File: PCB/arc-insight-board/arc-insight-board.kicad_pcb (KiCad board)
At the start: 2 copper layers, 14.1 x 69.5 mm, 41 parts, among them J1 USB_C_Receptacle, J2 Conn_01x06, J3 Conn_01x05, J4 Conn_01x02, J5 Conn_01x02, J6 FPC_24PIN, J7 Conn_01x02, J8 U.FL, M1 Electret, U1 ESP32-S3, U2 MAX98357A, U3 MAX98357A, U4 TP4054, U5 Comparator, U6 ME6211C33M5, Y1 40MHz

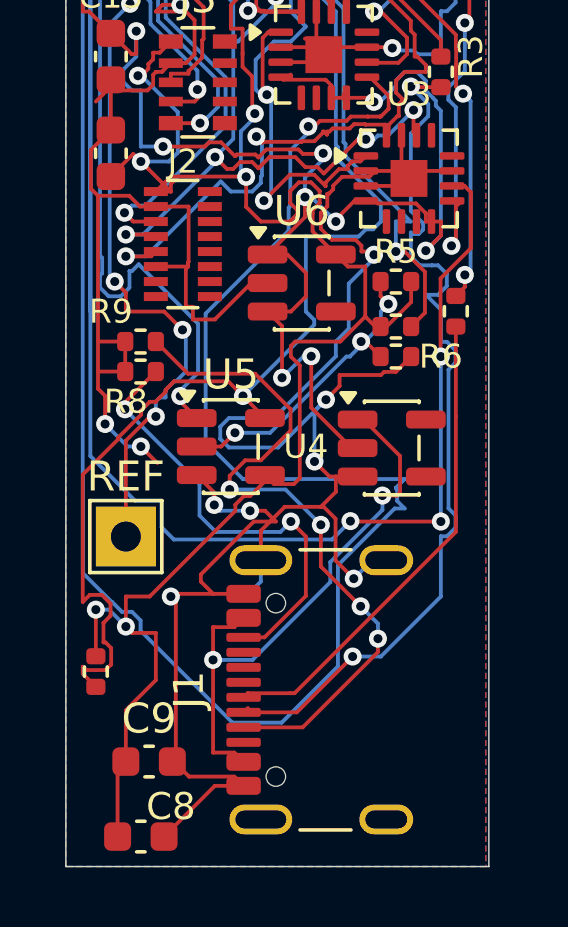
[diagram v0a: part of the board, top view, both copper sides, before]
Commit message: Fix J1 position, rotate U4/U6 to correct orientation
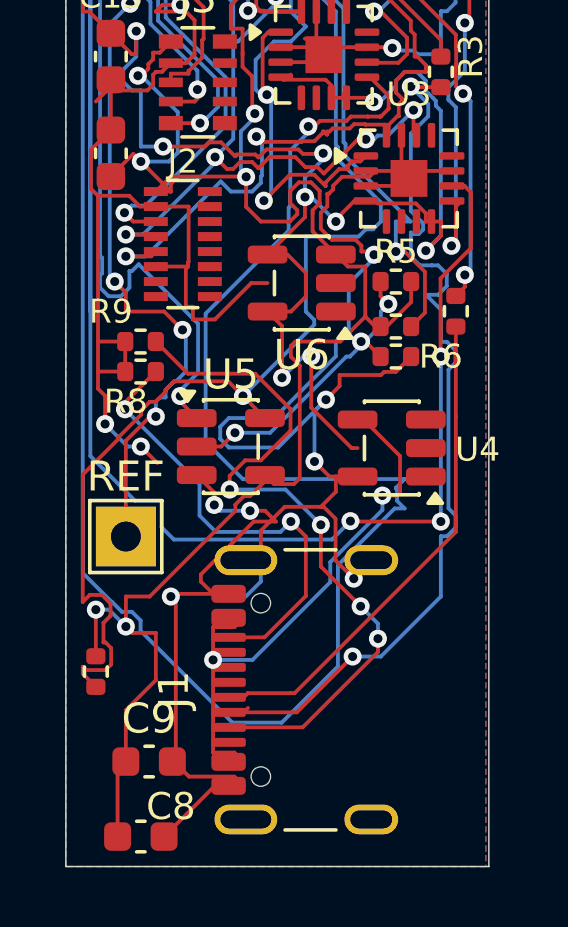
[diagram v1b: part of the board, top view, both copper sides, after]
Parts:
- moved J1 0.50 mm to (140.6, 136.6)
- turned U4 to 180 degrees
- turned U6 to 180 degrees
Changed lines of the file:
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@@
 	(footprint "Connector_USB:USB_C_Receptacle_GCT_USB4105-xx-A_16P_TopMnt_Horizontal"
 		(layer "F.Cu")
-		(at 141.105 136.61 90)
+		(at 140.605 136.61 90)
 		(descr "USB 2.0 Type C Receptacle, GCT, 16P, top mounted, horizontal, 5A: https://gct.co/files/drawings/usb4105.pdf")
 		(tags "USB C Type-C Receptacle SMD USB 2.0 16P 16C USB4105-15-A USB4105-15-A-060 USB4105-15-A-120 USB4105-GF-A USB4105-GF-A-060 USB4105-GF-A-120")
@@
 	(footprint "Package_TO_SOT_SMD:SOT-23-5"
 		(layer "F.Cu")
-		(at 142.3625 128.55)
+		(at 142.3625 128.55 180)
 		(descr "SOT, 5 Pin (JEDEC MO-178 Var AA https://www.jedec.org/document_search?search_api_views_fulltext=MO-178)")
 		(tags "SOT TO_SOT_SMD")
@@
 	(footprint "Package_TO_SOT_SMD:SOT-23-5"
 		(layer "F.Cu")
-		(at 139.3625 123.05)
+		(at 139.3625 123.05 180)
 		(descr "SOT, 5 Pin (JEDEC MO-178 Var AA https://www.jedec.org/document_search?search_api_views_fulltext=MO-178)")
 		(tags "SOT TO_SOT_SMD")

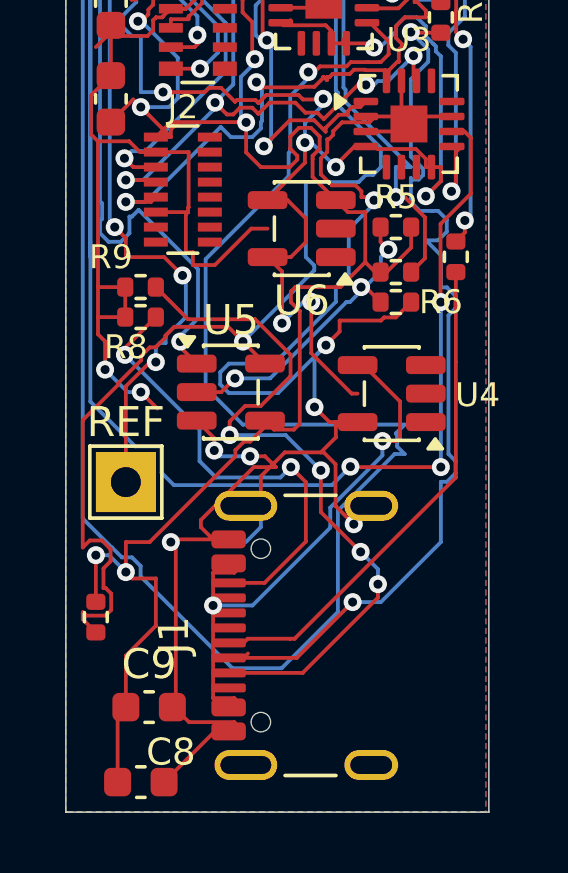
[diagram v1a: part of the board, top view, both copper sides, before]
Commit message: Adjust J1, U5, U6 rotations/position per request
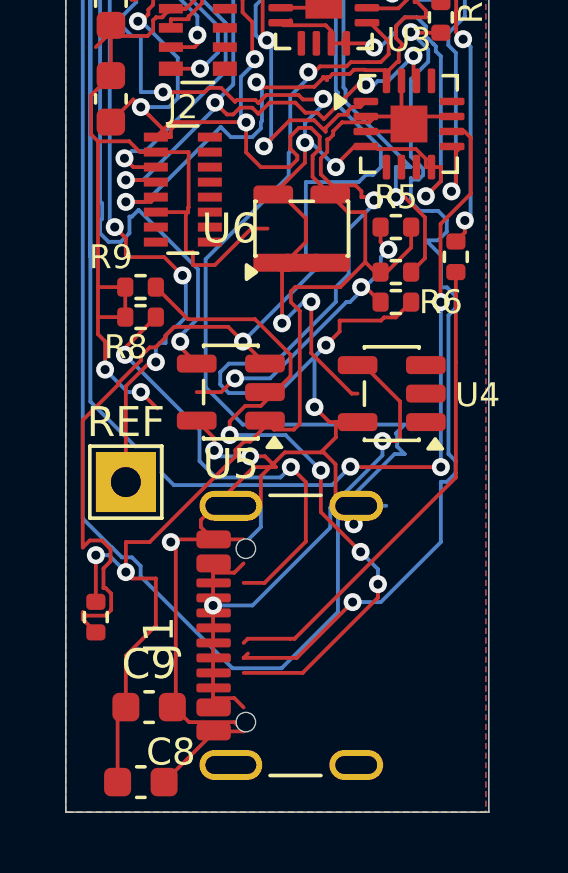
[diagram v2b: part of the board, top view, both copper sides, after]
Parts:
- moved J1 0.50 mm to (140.1, 136.6)
- turned U5 to 180 degrees
- turned U6 to 90 degrees
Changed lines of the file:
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@@
 	(footprint "Connector_USB:USB_C_Receptacle_GCT_USB4105-xx-A_16P_TopMnt_Horizontal"
 		(layer "F.Cu")
-		(at 140.605 136.61 90)
+		(at 140.105 136.61 90)
 		(descr "USB 2.0 Type C Receptacle, GCT, 16P, top mounted, horizontal, 5A: https://gct.co/files/drawings/usb4105.pdf")
 		(tags "USB C Type-C Receptacle SMD USB 2.0 16P 16C USB4105-15-A USB4105-15-A-060 USB4105-15-A-120 USB4105-GF-A USB4105-GF-A-060 USB4105-GF-A-120")
@@
 	(footprint "Package_TO_SOT_SMD:SOT-23-5"
 		(layer "F.Cu")
-		(at 139.3625 123.05 180)
+		(at 139.3625 123.05 90)
 		(descr "SOT, 5 Pin (JEDEC MO-178 Var AA https://www.jedec.org/document_search?search_api_views_fulltext=MO-178)")
 		(tags "SOT TO_SOT_SMD")
@@
 	(footprint "Package_TO_SOT_SMD:SOT-23-5"
 		(layer "F.Cu")
-		(at 137 128.5)
+		(at 137 128.5 180)
 		(descr "SOT, 5 Pin (JEDEC MO-178 Var AA https://www.jedec.org/document_search?search_api_views_fulltext=MO-178)")
 		(tags "SOT TO_SOT_SMD")

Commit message: Rotate U6 180 degrees
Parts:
- turned U6 to 270 degrees
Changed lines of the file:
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@@
 	(footprint "Package_TO_SOT_SMD:SOT-23-5"
 		(layer "F.Cu")
-		(at 139.3625 123.05 90)
+		(at 139.3625 123.05 270)
 		(descr "SOT, 5 Pin (JEDEC MO-178 Var AA https://www.jedec.org/document_search?search_api_views_fulltext=MO-178)")
 		(tags "SOT TO_SOT_SMD")

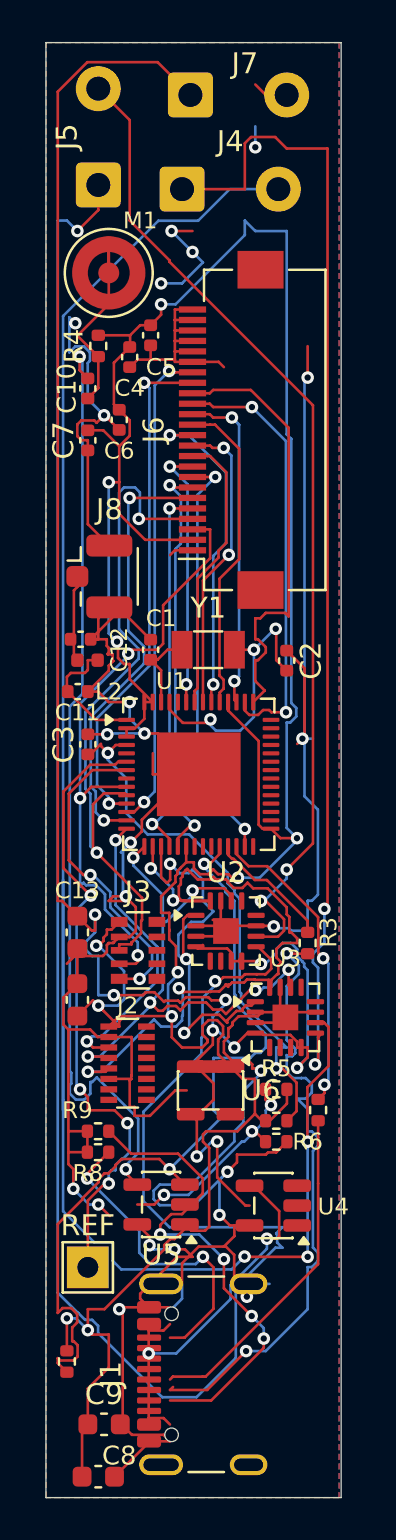
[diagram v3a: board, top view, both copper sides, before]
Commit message: Fix U1 (ESP32-S3FN8/C2913196) and Y1 (2520 4-pin crystal/C37635359); update BOMs, gerbers, positions
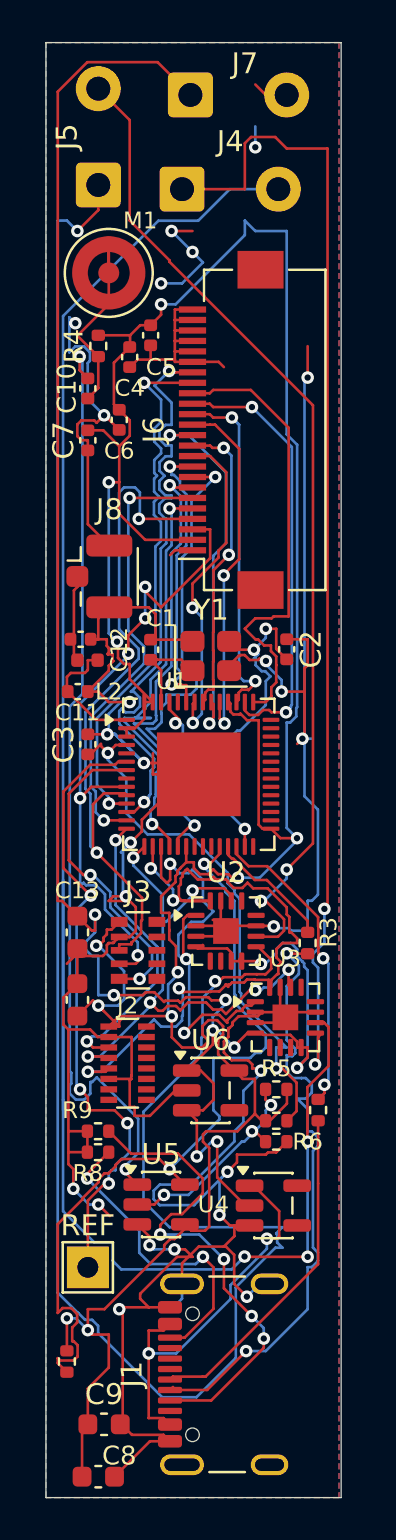
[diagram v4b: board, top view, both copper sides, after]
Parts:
- Y1: footprint Crystal:Crystal_SMD_3215-2Pin_3.2x1.5mm -> Crystal:Crystal_SMD_2520-4Pin_2.5x2.0mm
- moved J1 1.00 mm to (141.1, 136.6)
- moved C2 0.54 mm to (143.0, 102.0)
- moved Y1 0.32 mm to (139.4, 102.3), turned to 0 degrees
- turned U4 to 0 degrees
- turned U5 to 0 degrees
- turned U6 to 0 degrees
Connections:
- Y1 pad 2: /Net-XTAL_N -> GND
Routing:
- net GND: track 220.4 -> 232.0 mm, vias 23 -> 25
- net /Net-GPIO7: track 23.3 -> 28.7 mm
- net /Net-GPIO21: track 20.0 -> 23.9 mm
- net /Net-GPIO13: track 18.1 -> 21.6 mm
- net /Net-U0RXD: track 13.5 -> 16.1 mm, vias 0 -> 2
- net /Net-GPIO14: track 19.6 -> 21.9 mm
- net /Net-MTMS: track 15.8 -> 18.1 mm
- net /Net-MTDI: track 15.3 -> 17.5 mm, vias 0 -> 2
- net /Net-XTAL_N: track 13.3 -> 14.8 mm
- net /Net-J3Pin_4: track 30.0 -> 31.5 mm, vias 3 -> 5
- net /Net-GPIO6: track 24.6 -> 26.0 mm
- net /Net-GPIO45: track 12.7 -> 13.9 mm
- net /Net-MTDO: track 16.3 -> 17.4 mm
- net /Net-XTAL_P: track 3.93 -> 4.76 mm
- net /Net-GPIO38: track 21.2 -> 22.0 mm
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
